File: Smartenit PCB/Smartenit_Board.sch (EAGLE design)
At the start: 85 parts, among them J3 2X5CONNECTOR1.27MM, Q1 QUARTZ_3.58M_2PIN, U1 ADE7953, U2 ESP-WROOM-32, U3 SN74LVC1G3157

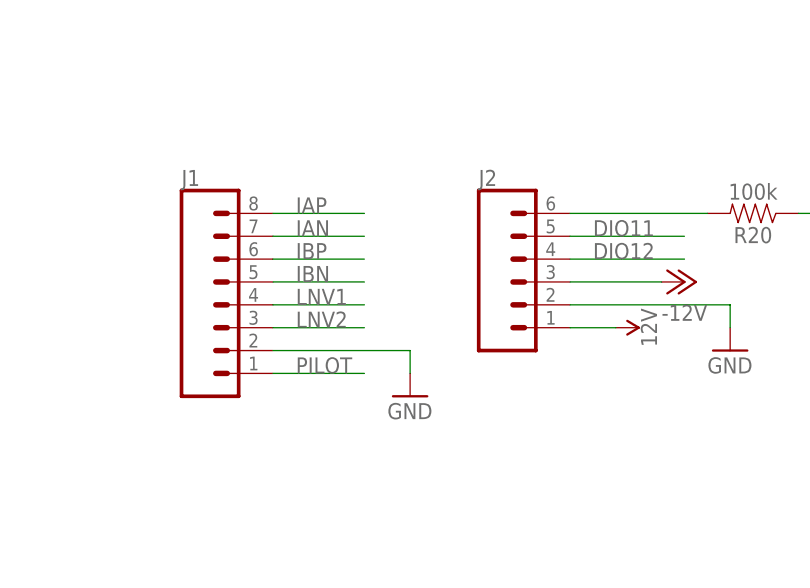
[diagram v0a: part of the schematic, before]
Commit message: update (google drive supported now)
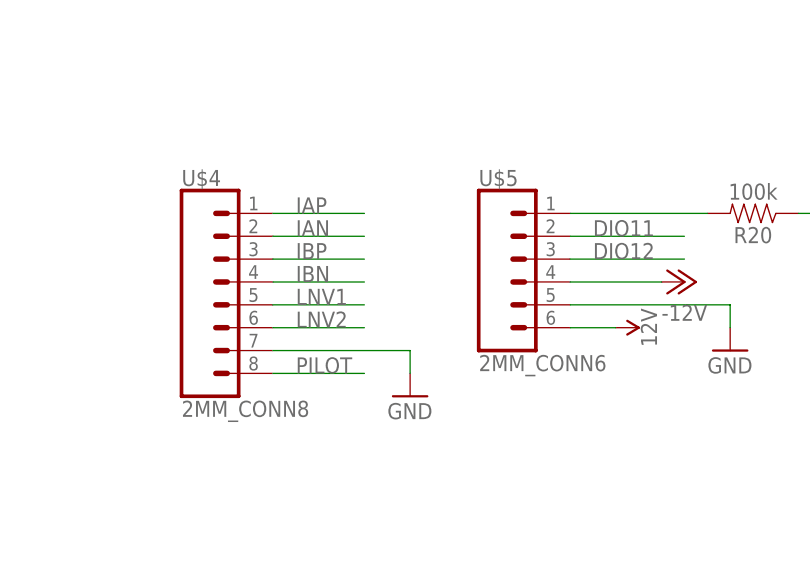
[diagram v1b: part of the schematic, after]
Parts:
- removed J1: (no value), SparkFun-Connectors:CONN_08"
- removed J2: (no value), SparkFun-Connectors:CONN_06SILK_FEMALE_PTH
- added U$4: 2MM_CONN8, Smart_Charger:2MM_CONN8
- added U$5: 2MM_CONN6, Smart_Charger:2MM_CONN6
- D5: device SparkFun:DIODE1N4148 -> SparkFun:DIODEHV
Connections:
- net -12V: now also U$5.PIN4; no longer J2.3
- net 12V: now also U$5.PIN6; no longer J2.1
- net DIO11: now also U$5.PIN2; no longer J2.5
- net DIO12: now also U$5.PIN3; no longer J2.4
- net GND: now also U$4.7, U$5.PIN5; no longer J1.2, J2.2
- net IAN: now also U$4.2; no longer J1.7
- net IAP: now also U$4.1; no longer J1.8
- net IBN: now also U$4.4; no longer J1.5
- net IBP: now also U$4.3; no longer J1.6
- net LNV1: now also U$4.5; no longer J1.4
- net LNV2: now also U$4.6; no longer J1.3
- net N$38: now also U$5.PIN1; no longer J2.6
- net PILOT: now also U$4.8; no longer J1.1

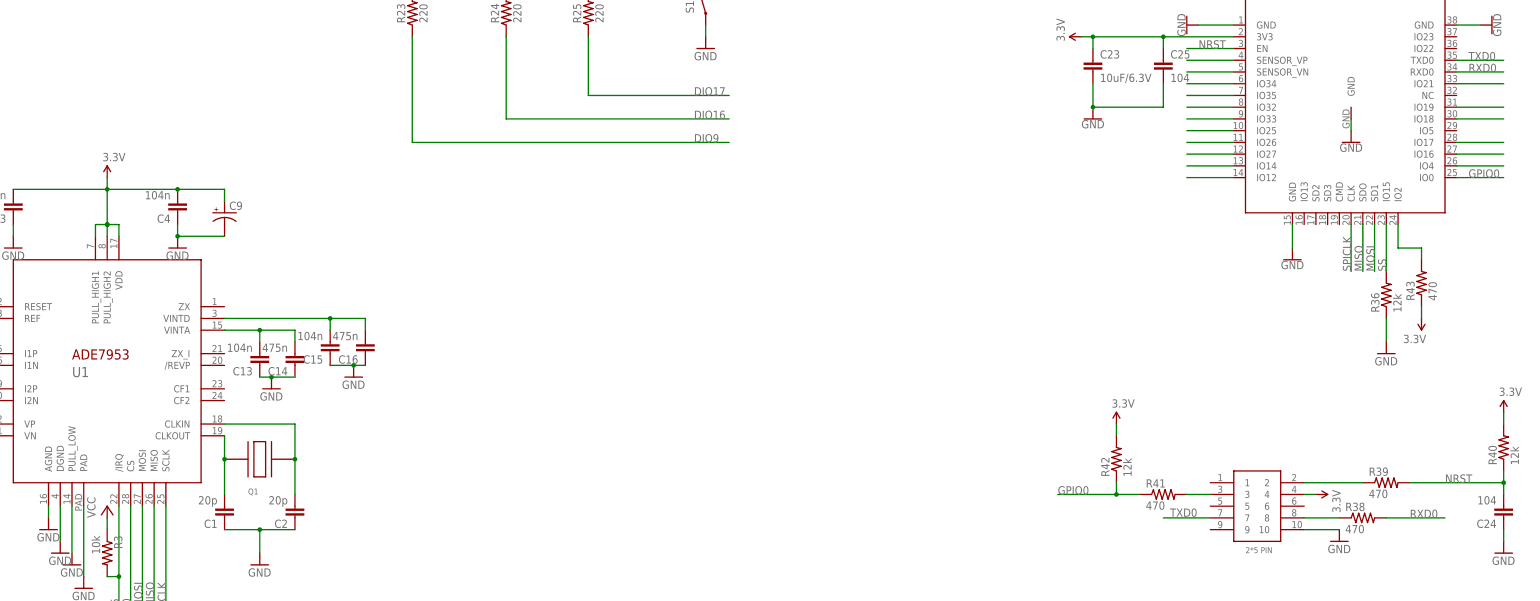
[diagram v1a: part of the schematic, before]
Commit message: routed board
routed and added pin connections to ESp module
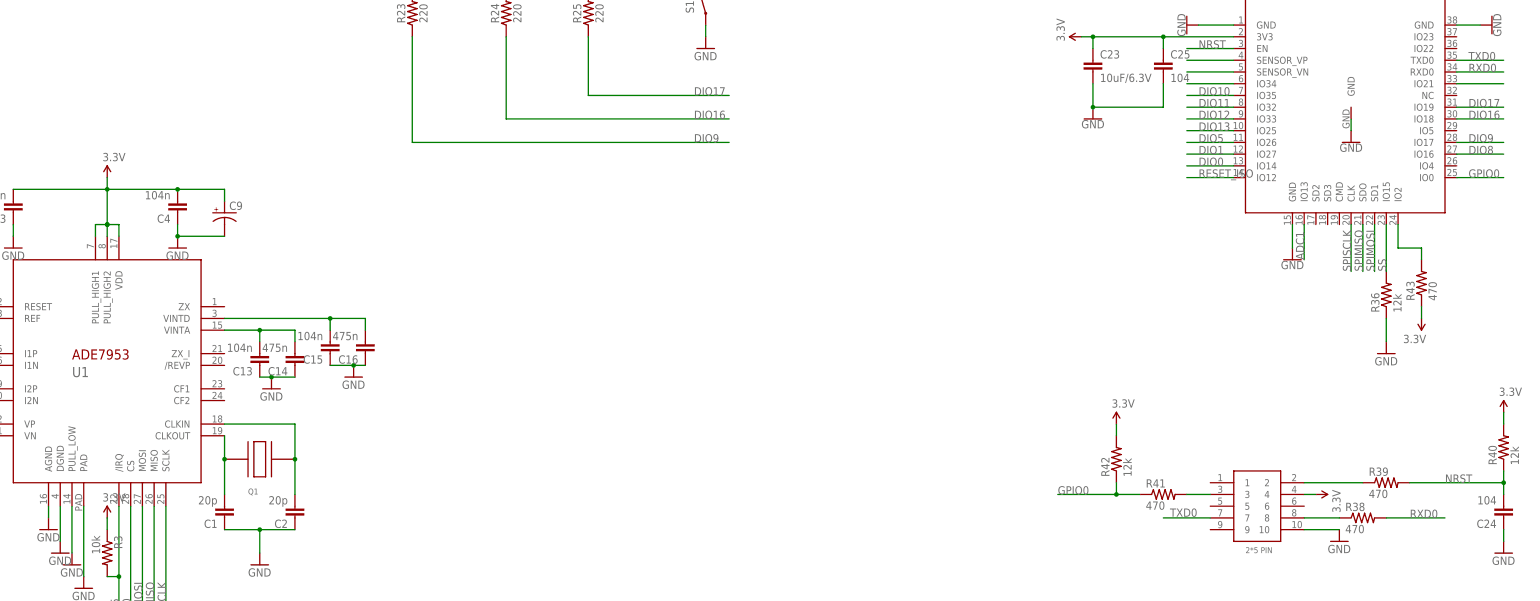
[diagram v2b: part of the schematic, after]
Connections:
- removed net MISO: U2.SDO
- removed net MOSI: U2.SD1
- removed net N$34: U2.IO12
- removed net N$35: U2.IO14
- removed net N$36: U2.IO27
- removed net N$37: U2.IO26
- removed net N$41: U2.IO25
- removed net N$42: U2.IO33
- removed net N$43: U2.IO32
- removed net N$44: U2.IO35
- removed net N$48: U2.IO18
- removed net N$49: U2.IO19
- removed net N$50: U2.IO17
- removed net N$51: U2.IO16
- removed net N$52: U2.IO4
- removed net SPICLK: U2.CLK
- removed net VCC: R3.1
- net 3.3V: now also R3.1
- net ADC1: now also U2.IO13
- net DIO0: now also U2.IO14
- net DIO1: now also U2.IO27
- net DIO10: now also U2.IO35
- net DIO11: now also U2.IO32
- net DIO12: now also U2.IO33
- net DIO13: now also U2.IO25
- net DIO16: now also U2.IO18
- net DIO17: now also U2.IO19
- net DIO5: now also U2.IO26
- net DIO8: now also U2.IO16
- net DIO9: now also U2.IO17
- net RESET_ISO: now also U2.IO12
- net SPIMISO: now also U2.SDO
- net SPIMOSI: now also U2.SD1
- net SPISCLK: now also U2.CLK

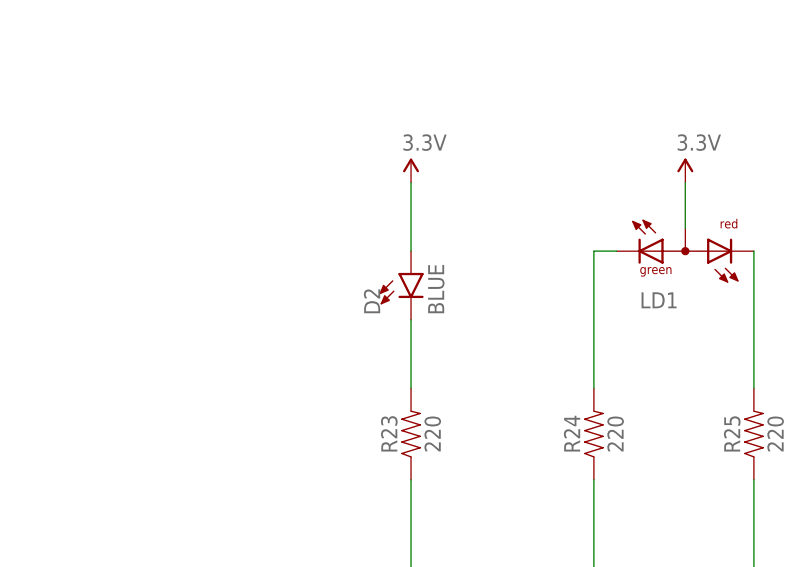
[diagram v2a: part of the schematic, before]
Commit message: changed blue LED
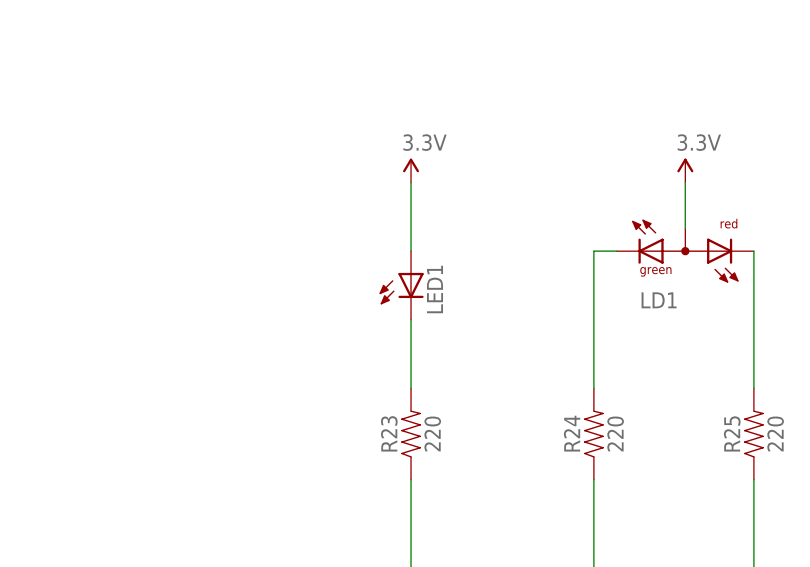
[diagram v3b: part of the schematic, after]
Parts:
- removed D2: BLUE, SparkFun-LED:LED-BLUE0603
- added LED1: (no value), SparkFun:LED3MM
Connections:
- net 3.3V: now also LED1.A; no longer D2.A
- net N$21: now also LED1.C; no longer D2.C
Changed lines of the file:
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@@
 <grid distance="0.1" unitdist="inch" unit="inch" style="lines" multiple="1" display="no" altdistance="0.01" altunitdist="inch" altunit="inch"/>
 <layers>
-<layer number="1" name="Top" color="4" fill="1" visible="no" active="no"/>
-<layer number="2" name="Route2" color="1" fill="3" visible="no" active="no"/>
-<layer number="3" name="Route3" color="4" fill="3" visible="no" active="no"/>
-<layer number="4" name="Route4" color="1" fill="4" visible="no" active="no"/>
-<layer number="5" name="Route5" color="4" fill="4" visible="no" active="no"/>
-<layer number="6" name="Route6" color="1" fill="8" visible="no" active="no"/>
-<layer number="7" name="Route7" color="4" fill="8" visible="no" active="no"/>
-<layer number="8" name="Route8" color="1" fill="2" visible="no" active="no"/>
-<layer number="9" name="Route9" color="4" fill="2" visible="no" active="no"/>
-<layer number="10" name="Route10" color="1" fill="7" visible="no" active="no"/>
-<layer number="11" name="Route11" color="4" fill="7" visible="no" active="no"/>
-<layer number="12" name="Route12" color="1" fill="5" visible="no" active="no"/>
-<layer number="13" name="Route13" color="4" fill="5" visible="no" active="no"/>
-<layer number="14" name="Route14" color="1" fill="6" visible="no" active="no"/>
-<layer number="15" name="Route15" color="4" fill="6" visible="no" active="no"/>
-<layer number="16" name="Bottom" color="1" fill="1" visible="no" active="no"/>
-<layer number="17" name="Pads" color="2" fill="1" visible="no" active="no"/>
-<layer number="18" name="Vias" color="2" fill="1" visible="no" active="no"/>
-<layer number="19" name="Unrouted" color="6" fill="1" visible="no" active="no"/>
-<layer number="20" name="Dimension" color="15" fill="1" visible="no" active="no"/>
-<layer number="21" name="tPlace" color="7" fill="1" visible="no" active="no"/>
-<layer number="22" name="bPlace" color="7" fill="1" visible="no" active="no"/>
-<layer number="23" name="tOrigins" color="15" fill="1" visible="no" active="no"/>
-<layer number="24" name="bOrigins" color="15" fill="1" visible="no" active="no"/>
-<layer number="25" name="tNames" color="7" fill="1" visible="no" active="no"/>
-<layer number="26" name="bNames" color="7" fill="1" visible="no" active="no"/>
-<layer number="27" name="tValues" color="7" fill="1" visible="no" active="no"/>
-<layer number="28" name="bValues" color="7" fill="1" visible="no" active="no"/>
+<layer number="1" name="Top" color="4" fill="1" visible="yes" active="no"/>
+<layer number="2" name="Route2" color="1" fill="3" visible="yes" active="no"/>
+<layer number="3" name="Route3" color="4" fill="3" visible="yes" active="no"/>
+<layer number="4" name="Route4" color="1" fill="4" visible="yes" active="no"/>
+<layer number="5" name="Route5" color="4" fill="4" visible="yes" active="no"/>
+<layer number="6" name="Route6" color="1" fill="8" visible="yes" active="no"/>
+<layer number="7" name="Route7" color="4" fill="8" visible="yes" active="no"/>
+<layer number="8" name="Route8" color="1" fill="2" visible="yes" active="no"/>
+<layer number="9" name="Route9" color="4" fill="2" visible="yes" active="no"/>
+<layer number="10" name="Route10" color="1" fill="7" visible="yes" active="no"/>
+<layer number="11" name="Route11" color="4" fill="7" visible="yes" active="no"/>
+<layer number="12" name="Route12" color="1" fill="5" visible="yes" active="no"/>
+<layer number="13" name="Route13" color="4" fill="5" visible="yes" active="no"/>
+<layer number="14" name="Route14" color="1" fill="6" visible="yes" active="no"/>
+<layer number="15" name="Route15" color="4" fill="6" visible="yes" active="no"/>
+<layer number="16" name="Bottom" color="1" fill="1" visible="yes" active="no"/>
+<layer number="17" name="Pads" color="2" fill="1" visible="yes" active="no"/>
+<layer number="18" name="Vias" color="2" fill="1" visible="yes" active="no"/>
+<layer number="19" name="Unrouted" color="6" fill="1" visible="yes" active="no"/>
+<layer number="20" name="Dimension" color="15" fill="1" visible="yes" active="no"/>
+<layer number="21" name="tPlace" color="7" fill="1" visible="yes" active="no"/>
+<layer number="22" name="bPlace" color="7" fill="1" visible="yes" active="no"/>
+<layer number="23" name="tOrigins" color="15" fill="1" visible="yes" active="no"/>
+<layer number="24" name="bOrigins" color="15" fill="1" visible="yes" active="no"/>
+<layer number="25" name="tNames" color="7" fill="1" visible="yes" active="no"/>
+<layer number="26" name="bNames" color="7" fill="1" visible="yes" active="no"/>
+<layer number="27" name="tValues" color="7" fill="1" visible="yes" active="no"/>
+<layer number="28" name="bValues" color="7" fill="1" visible="yes" active="no"/>
 <layer number="29" name="tStop" color="7" fill="3" visible="no" active="no"/>
 <layer number="30" name="bStop" color="7" fill="6" visible="no" active="no"/>
@@
 <layer number="35" name="tGlue" color="7" fill="4" visible="no" active="no"/>
 <layer number="36" name="bGlue" color="7" fill="5" visible="no" active="no"/>
-<layer number="37" name="tTest" color="7" fill="1" visible="no" active="no"/>
-<layer number="38" name="bTest" color="7" fill="1" visible="no" active="no"/>
+<layer number="37" name="tTest" color="7" fill="1" visible="yes" active="no"/>
+<layer number="38" name="bTest" color="7" fill="1" visible="yes" active="no"/>
 <layer number="39" name="tKeepout" color="4" fill="11" visible="no" active="no"/>
 <layer number="40" name="bKeepout" color="1" fill="11" visible="no" active="no"/>
@@
 <layer number="44" name="Drills" color="7" fill="1" visible="no" active="no"/>
 <layer number="45" name="Holes" color="7" fill="1" visible="no" active="no"/>
-<layer number="46" name="Milling" color="3" fill="1" visible="no" active="no"/>
-<layer number="47" name="Measures" color="7" fill="1" visible="no" active="no"/>
-<layer number="48" name="Document" color="7" fill="1" visible="no" active="no"/>
-<layer number="49" name="Reference" color="14" fill="1" visible="no" active="no"/>
-<layer number="50" name="dxf" color="7" fill="1" visible="no" active="no"/>
-<layer number="51" name="tDocu" color="6" fill="1" visible="no" active="no"/>
-<layer number="52" name="bDocu" color="6" fill="1" visible="no" active="no"/>
-<layer number="53" name="tGND_GNDA" color="7" fill="9" visible="no" active="no"/>
-<layer number="54" name="bGND_GNDA" color="1" fill="9" visible="no" active="no"/>
-<layer number="56" name="wert" color="7" fill="1" visible="no" active="no"/>
-<layer number="57" name="tCAD" color="7" fill="1" visible="no" active="no"/>
-<layer number="59" name="tCarbon" color="7" fill="1" visible="no" active="no"/>
-<layer number="60" name="bCarbon" color="7" fill="1" visible="no" active="no"/>
+<layer number="46" name="Milling" color="3" fill="1" visible="yes" active="no"/>
+<layer number="47" name="Measures" color="7" fill="1" visible="yes" active="no"/>
+<layer number="48" name="Document" color="7" fill="1" visible="yes" active="no"/>
+<layer number="49" name="Reference" color="14" fill="1" visible="yes" active="no"/>
+<layer number="50" name="dxf" color="7" fill="1" visible="yes" active="no"/>
+<layer number="51" name="tDocu" color="6" fill="1" visible="yes" active="no"/>
+<layer number="52" name="bDocu" color="6" fill="1" visible="yes" active="no"/>
+<layer number="53" name="tGND_GNDA" color="7" fill="9" visible="yes" active="no"/>
+<layer number="54" name="bGND_GNDA" color="1" fill="9" visible="yes" active="no"/>
+<layer number="56" name="wert" color="7" fill="1" visible="yes" active="no"/>
+<layer number="57" name="tCAD" color="7" fill="1" visible="yes" active="no"/>
+<layer number="59" name="tCarbon" color="7" fill="1" visible="yes" active="no"/>
+<layer number="60" name="bCarbon" color="7" fill="1" visible="yes" active="no"/>
 <layer number="88" name="SimResults" color="9" fill="1" visible="no" active="yes"/>
 <layer number="89" name="SimProbes" color="9" fill="1" visible="no" active="yes"/>
@@
 <part name="P+4" library="SparkFun" deviceset="3.3V" device=""/>
 <part name="P+1" library="SparkFun" deviceset="3.3V" device=""/>
-<part name="D2" library="SparkFun-LED" deviceset="LED-BLUE" device="0603" value="BLUE"/>
 <part name="R21" library="SparkFun-Resistors" deviceset="10KOHM" device="-0603-1/10W-1%" value="10k"/>
 <part name="R23" library="SparkFun-Resistors" deviceset="10KOHM" device="-0603-1/10W-1%" value="220"/>
@@
 <part name="U$5" library="Smart_Charger" deviceset="2MM_CONN6" device=""/>
 <part name="P+16" library="SparkFun" deviceset="3.3V" device=""/>
+<part name="LED1" library="SparkFun" deviceset="LED" device="3MM"/>
 </parts>
 <sheets>
@@
 <instance part="P+4" gate="G$1" x="-259.08" y="71.12"/>
 <instance part="P+1" gate="G$1" x="-200.66" y="7.62"/>
-<instance part="D2" gate="G$1" x="-134.62" y="60.96"/>
 <instance part="R21" gate="G$1" x="-71.12" y="58.42" rot="R90"/>
 <instance part="R23" gate="G$1" x="-134.62" y="43.18" rot="R90"/>
@@
 <instance part="U$5" gate="G$1" x="-294.64" y="40.64"/>
 <instance part="P+16" gate="G$1" x="-200.66" y="-66.04"/>
+<instance part="LED1" gate="G$1" x="-134.62" y="60.96"/>
 </instances>
 <busses>
@@
 <segment>
 <pinref part="P+5" gate="G$1" pin="3.3V"/>
-<pinref part="D2" gate="G$1" pin="A"/>
 <wire x1="-134.62" y1="71.12" x2="-134.62" y2="63.5" width="0.1524" layer="91"/>
+<pinref part="LED1" gate="G$1" pin="A"/>
 </segment>
 <segment>
@@
 <net name="N$21" class="0">
 <segment>
-<pinref part="D2" gate="G$1" pin="C"/>
 <pinref part="R23" gate="G$1" pin="2"/>
 <wire x1="-134.62" y1="55.88" x2="-134.62" y2="48.26" width="0.1524" layer="91"/>
-</segment>
-</net>
+<pinref part="LED1" gate="G$1" pin="C"/>
+</segment>
+</net>

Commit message: Finished Routing
Finished aligning dimensions, routing, fixing trace sizes and fixed cap on 12V line.
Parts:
- added C26: (no value), SparkFun:CAP_POLPTH1
- C9: device SparkFun:CAP_POLPTH2 -> SparkFun:CAP_POL1206
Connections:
- net 12V: now also C26.+
- net GND: now also C26.-
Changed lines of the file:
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@@
 <part name="C4" library="Nizanlib" deviceset="0402-CAP" device="" value="104n"/>
 <part name="GNDI3" library="SparkFun" deviceset="GND" device=""/>
-<part name="C9" library="SparkFun" deviceset="CAP_POL" device="PTH2"/>
+<part name="C9" library="SparkFun" deviceset="CAP_POL" device="1206"/>
 <part name="U$1" library="Smart_Charger" deviceset="MP1584" device=""/>
 <part name="GNDI4" library="SparkFun" deviceset="GND" device=""/>
@@
 <part name="P+16" library="SparkFun" deviceset="3.3V" device=""/>
 <part name="LED1" library="SparkFun" deviceset="LED" device="3MM"/>
+<part name="C26" library="SparkFun" deviceset="CAP_POL" device="PTH1"/>
+<part name="GNDI28" library="SparkFun" deviceset="GND" device=""/>
 </parts>
 <sheets>
@@
 <instance part="P+16" gate="G$1" x="-200.66" y="-66.04"/>
 <instance part="LED1" gate="G$1" x="-134.62" y="60.96"/>
+<instance part="C26" gate="G$1" x="-177.8" y="157.48"/>
+<instance part="GNDI28" gate="1" x="-177.8" y="137.16"/>
 </instances>
 <busses>
@@
 <wire x1="-160.02" y1="165.1" x2="-160.02" y2="160.02" width="0.1524" layer="91"/>
 <junction x="-160.02" y="165.1"/>
+<pinref part="C26" gate="G$1" pin="+"/>
+<wire x1="-177.8" y1="160.02" x2="-177.8" y2="165.1" width="0.1524" layer="91"/>
+<wire x1="-177.8" y1="165.1" x2="-160.02" y2="165.1" width="0.1524" layer="91"/>
 </segment>
 <segment>
@@
 <wire x1="76.2" y1="-27.94" x2="76.2" y2="-22.86" width="0.1524" layer="91"/>
 </segment>
-</net>
+<segment>
+<pinref part="GNDI28" gate="1" pin="GND"/>
+<pinref part="C26" gate="G$1" pin="-"/>
+<wire x1="-177.8" y1="139.7" x2="-177.8" y2="152.4" width="0.1524" layer="91"/>
+</segment>
+</net>
